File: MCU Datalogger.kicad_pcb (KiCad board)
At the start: 2 copper layers, 50.2 x 35.6 mm, 30 parts, among them J1 Conn_01x04_Pin, J2 Conn_01x04_Pin, J3 Conn_01x09_Pin, J4 Conn_02x03_Odd_Even, U1 24LC1025, U2 24LC1025, U3 DS1337S_, U4 ATMEGA328P-AU, Y1 16 MHz, Y2 32.768 KHz

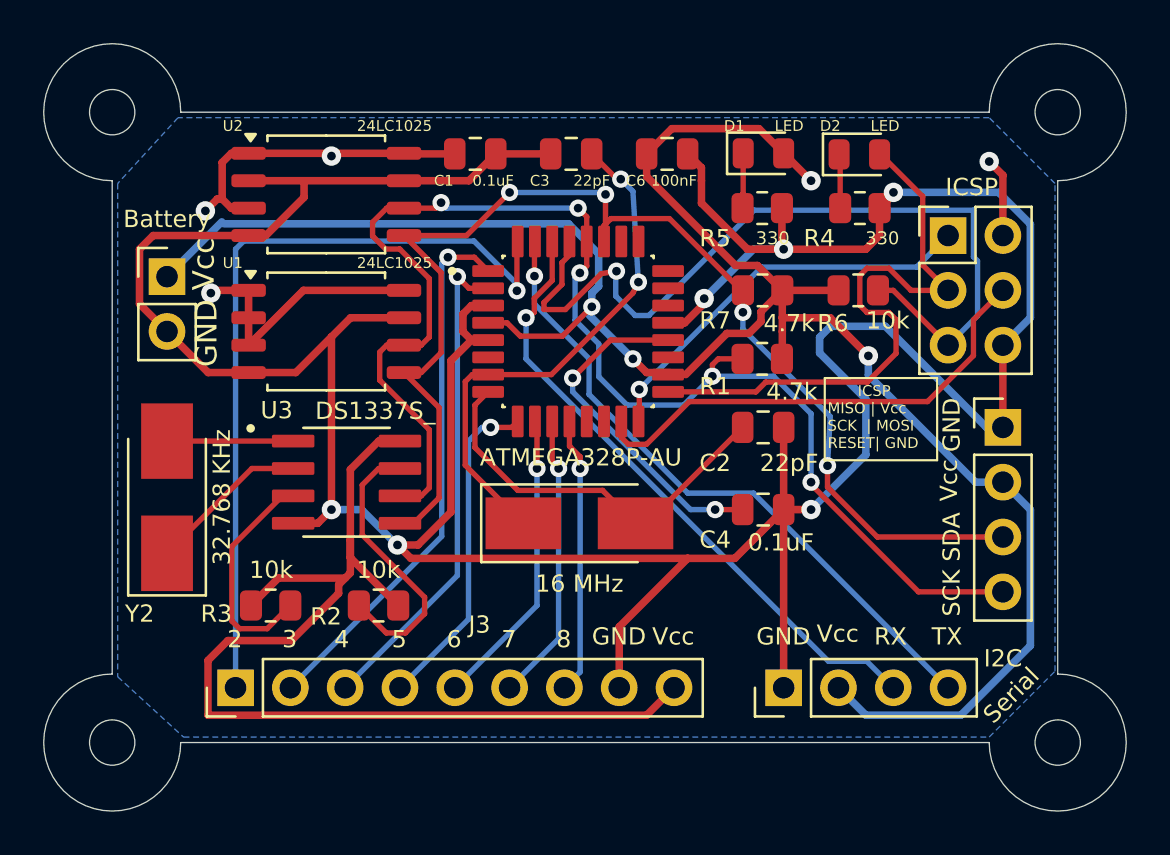
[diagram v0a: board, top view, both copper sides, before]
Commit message: Completed 4 Layer PCB Routing.
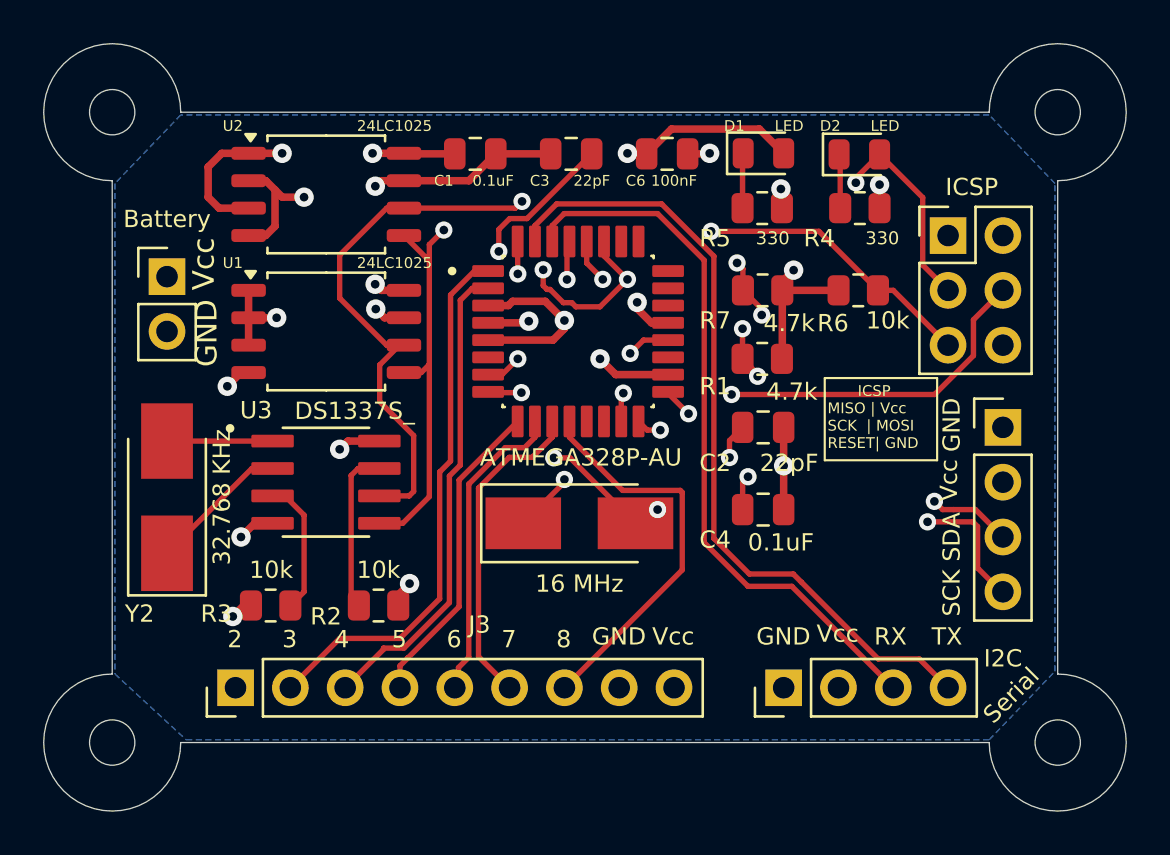
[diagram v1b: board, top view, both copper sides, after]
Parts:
- moved U3 0.95 mm to (72.0, 104.1)
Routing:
- net /Vcc: track 181.1 -> 41.1 mm, vias 8 -> 11
- net GND: track 170.1 -> 36.1 mm, vias 6 -> 11
- net /RESET: track 39.0 -> 22.6 mm, vias 1 -> 2
- net /D2: track 37.0 -> 28.9 mm
- net /TX: track 30.4 -> 37.2 mm, vias 1 -> 0
- net Net-(U3-SQW/~INT): track 13.2 -> 7.62 mm
- net /D8: track 12.8 -> 18.3 mm, vias 1 -> 0
- net /SCL: track 64.7 -> 59.9 mm
- net Net-(U3-~{INTA}): track 10.6 -> 6.28 mm
- net /RX: track 29.3 -> 33.5 mm, vias 1 -> 0
- net /SCK: track 28.5 -> 24.7 mm, vias 0 -> 2
- net /SDA: track 58.5 -> 56.1 mm, vias 4 -> 6
- net Net-(U4-AREF): track 15.9 -> 13.9 mm
- net /D7: track 13.4 -> 15.0 mm, vias 1 -> 0
- net Net-(U4-PB6): track 24.6 -> 23.3 mm, vias 2 -> 3
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- added copper zone on In1.Cu, net /Vcc
- added copper zone on B.Cu, net GND
- removed copper zone on B.Cu, net /Vcc
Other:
- copper layers 2 -> 4
